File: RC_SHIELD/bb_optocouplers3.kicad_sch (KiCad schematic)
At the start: 41 parts, among them U1 SFH6345, U10 SFH6345, U11 SFH6345, U2 SFH6345, U9 SFH6345

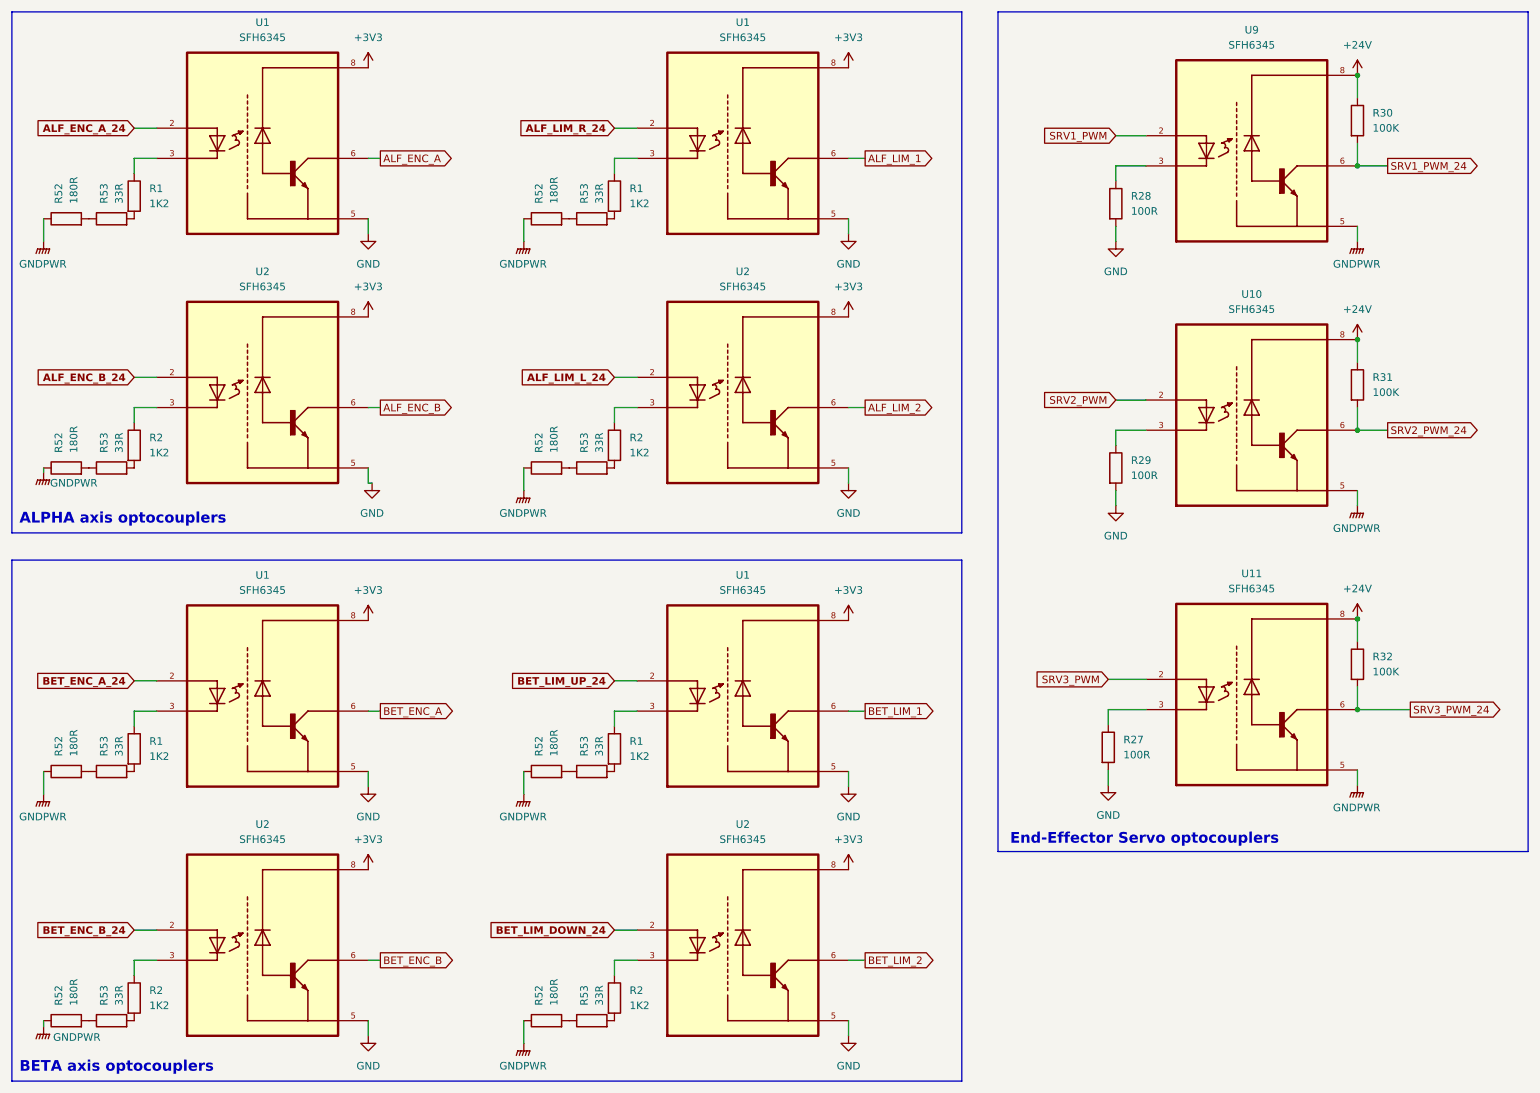
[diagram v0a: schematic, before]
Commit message: [SCH] reannotated entire schematic so PCBnew wont complain
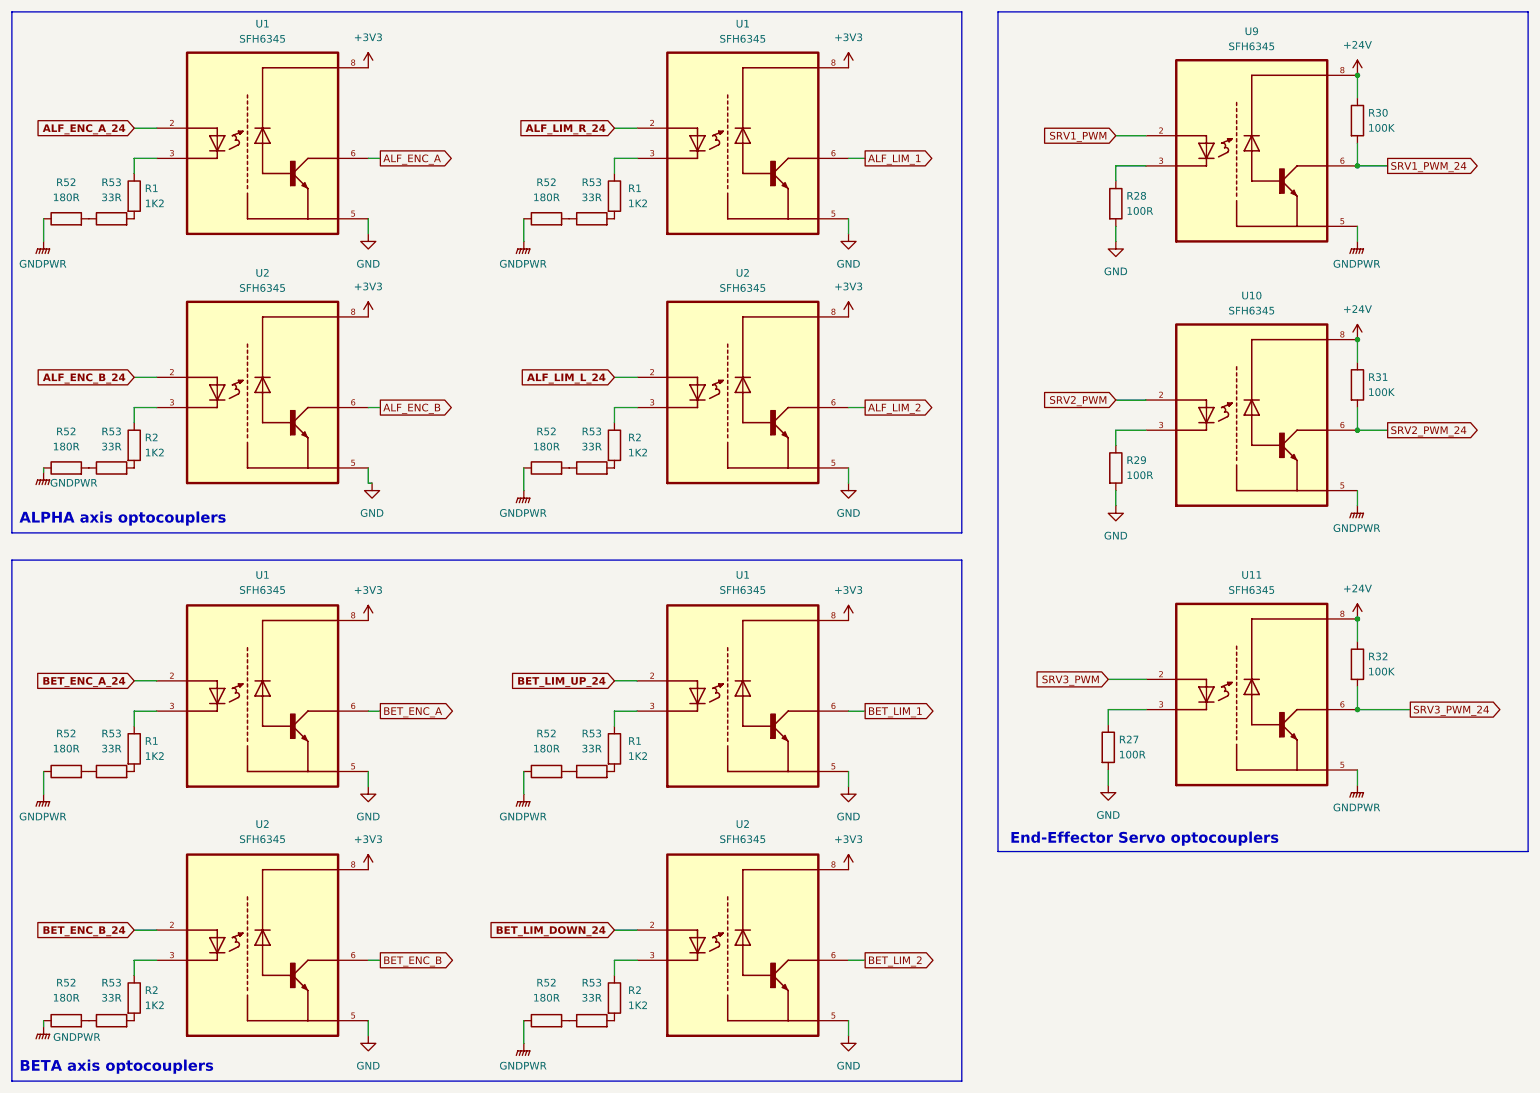
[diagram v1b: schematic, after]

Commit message: Revert "[SCH] reannotated entire schematic so PCBnew wont complain"
This reverts commit df148950bb8496d2d5af5a937770664cb0004a0d.
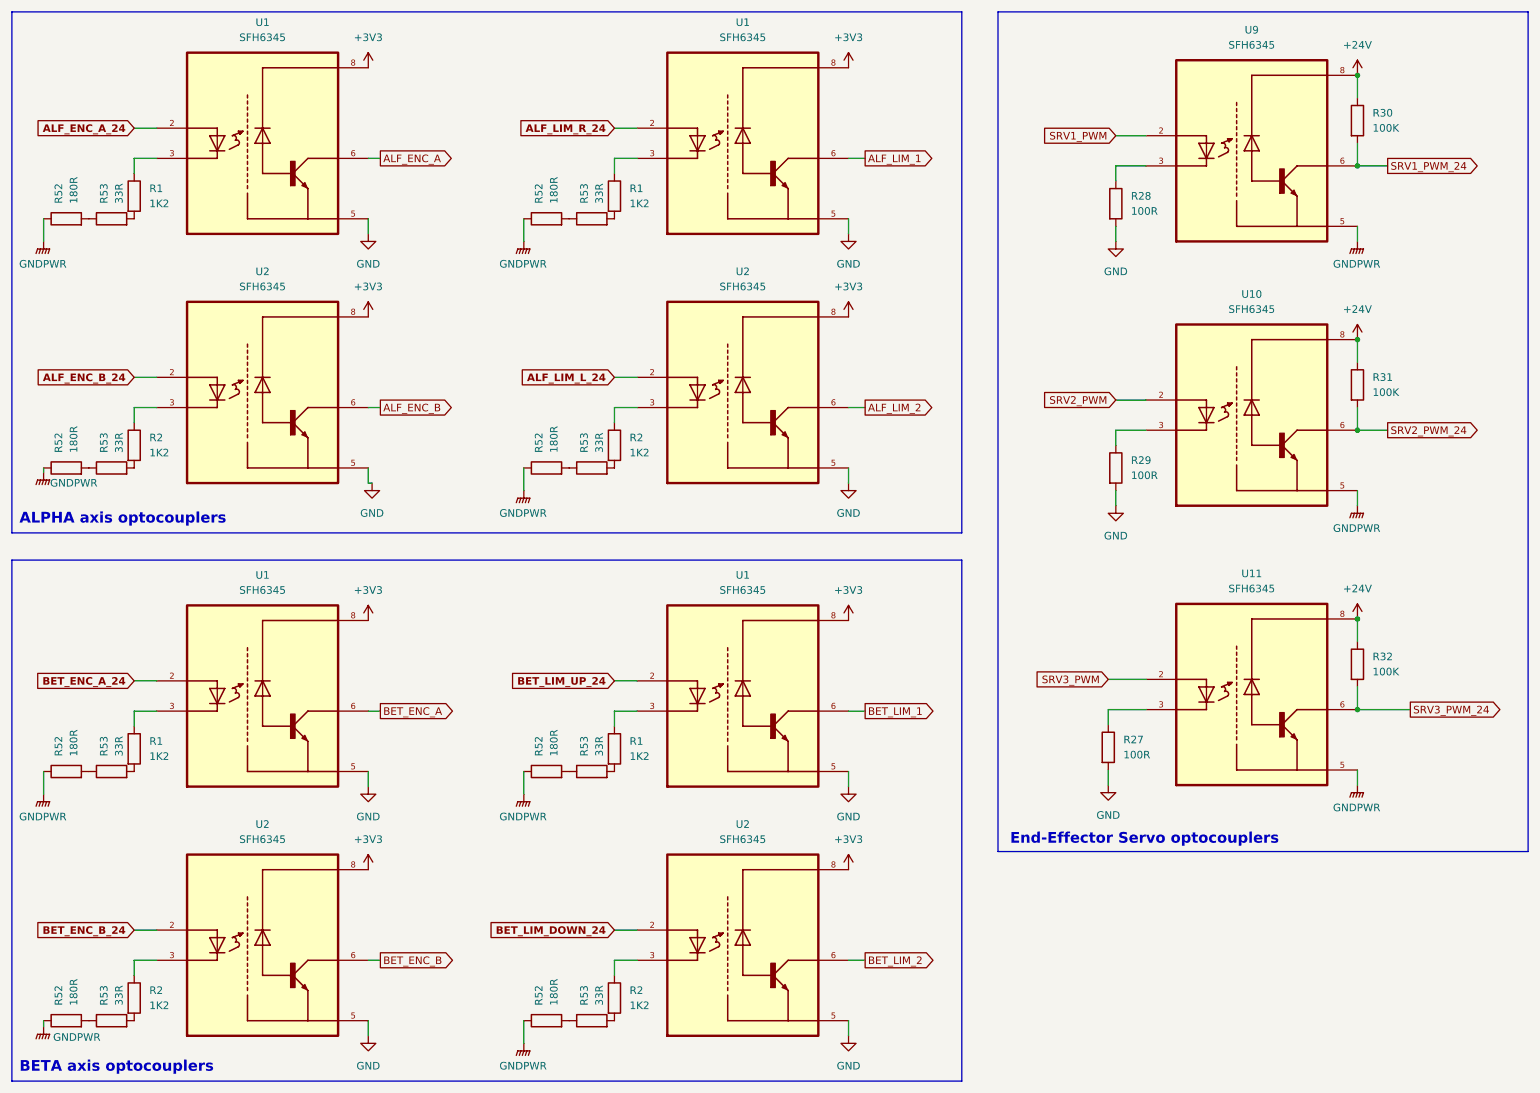
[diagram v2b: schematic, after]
